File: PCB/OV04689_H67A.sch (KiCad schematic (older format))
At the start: 47 parts

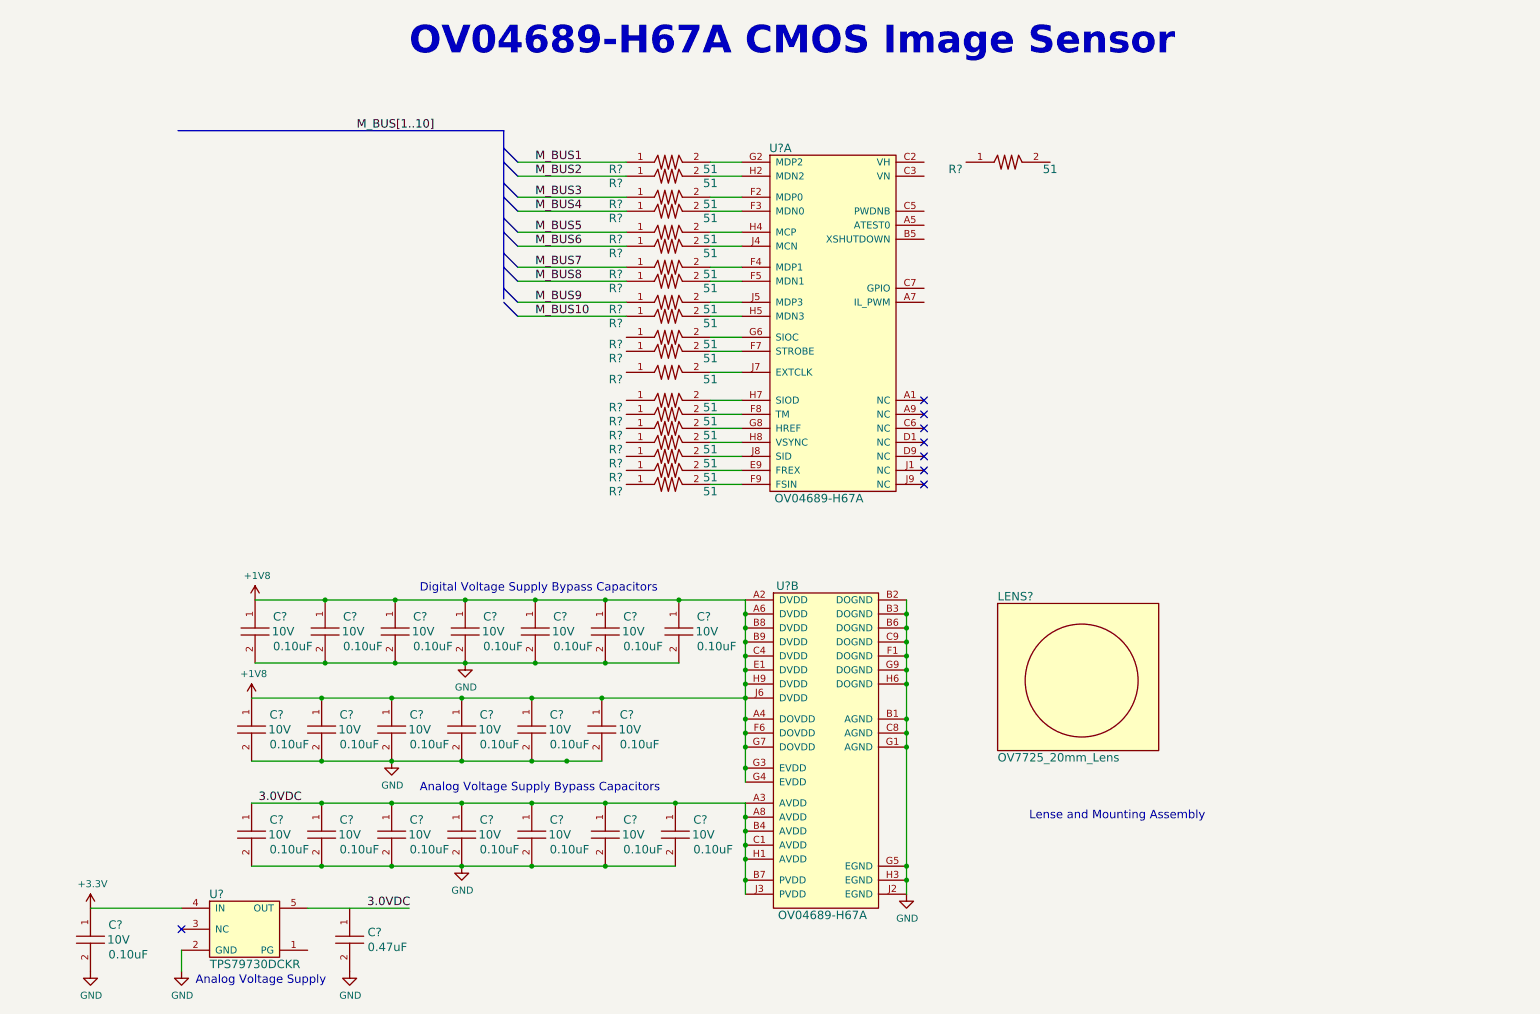
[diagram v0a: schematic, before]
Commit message: Memory and Camera
Memory and Camera schematics tentatively complete. They are subject to
change as all hardware projects are.
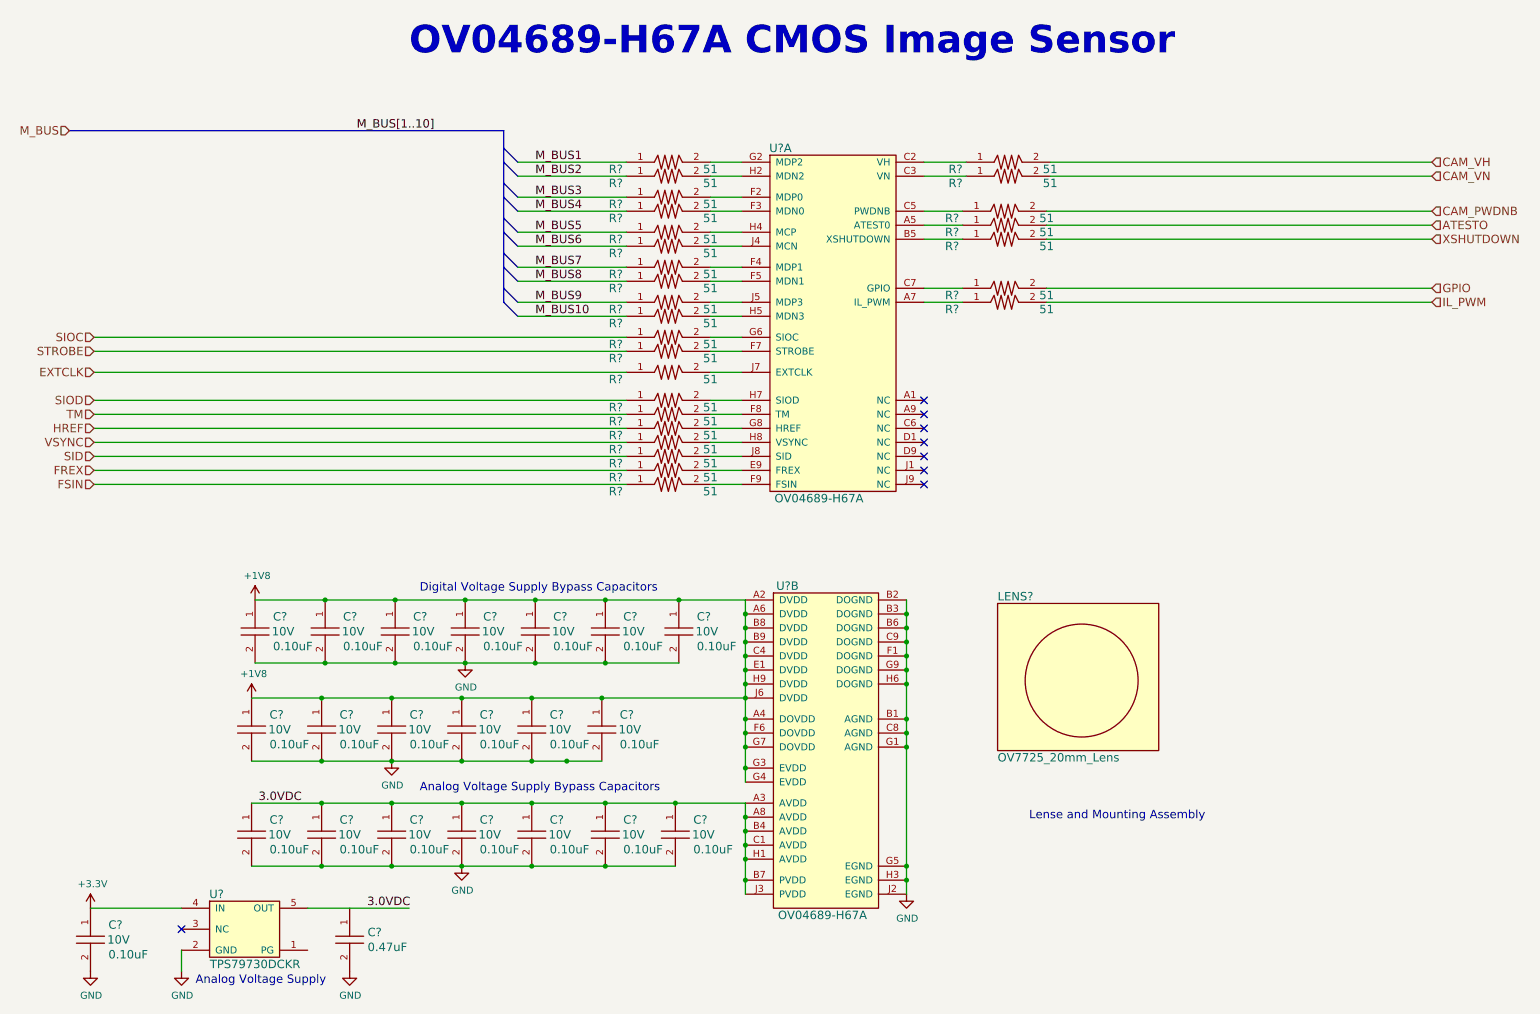
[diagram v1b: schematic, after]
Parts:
- added R? (x6): RC1005F510CS, PCB_Footprints:R0402, symbol RC1005F510CS
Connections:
- net labels added: ATESTO, CAM_PWDNB, CAM_VH, CAM_VN, EXTCLK, FREX, FSIN, GPIO, HREF, IL_PWM, M_BUS, SID, SIOC, SIOD, STROBE, TM, VSYNC, XSHUTDOWN
- wire segments 42 -> 66
